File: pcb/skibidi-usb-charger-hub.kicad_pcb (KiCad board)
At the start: 4 copper layers, 85 x 90 mm, 92 parts, among them J1 USB_C_Receptacle_USB2.0_14P, J2 USB_C_Receptacle_USB2.0_14P, J3 USB_C_Receptacle_USB2.0_14P, J4 USB_C_Receptacle_USB2.0_14P, J5 USB_C_Receptacle_USB2.0_14P, J6 USB_C_Receptacle_USB2.0_14P, U10 IP6518, U11 USBLC6-4SC6, U12 IP6518, U13 USBLC6-4SC6, U14 IP6518, U15 USBLC6-4SC6, U16 IP6518, U17 USBLC6-4SC6, U3 NDP5102SE, U6 NDP5102SE, U9 NDP5102SE

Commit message: update art + gerbers + readme
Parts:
- added H23: 5V, extras:18AWG_Soldering_Hole, F.Cu at (125.0, 95.0)
- added H24: 5V, extras:18AWG_Soldering_Hole, F.Cu at (132.0, 95.0)
- added H25: 5V, extras:18AWG_Soldering_Hole, F.Cu at (139.0, 95.0)
- added H26: 12V, extras:18AWG_Soldering_Hole, F.Cu at (154.0, 95.0)
- added H27: 12V, extras:18AWG_Soldering_Hole, F.Cu at (161.0, 95.0)
- added H28: 12V, extras:18AWG_Soldering_Hole, F.Cu at (168.0, 95.0)
- added J10: Conn_02x01, Connector_PinHeader_2.54mm:PinHeader_2x01_P2.54mm_Vertical, F.Cu at (97.0, 64.0)
- added J7: Conn_02x01, Connector_PinHeader_2.54mm:PinHeader_2x01_P2.54mm_Vertical, F.Cu at (135.0, 138.0)
- added J8: Conn_02x01, Connector_PinHeader_2.54mm:PinHeader_2x01_P2.54mm_Vertical, F.Cu at (154.0, 138.0)
- added J9: Conn_02x01, Connector_PinHeader_2.54mm:PinHeader_2x01_P2.54mm_Vertical, F.Cu at (97.0, 84.0)
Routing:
- added copper zone on F.Cu, net GND
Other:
- board text added: "12V"
- board text added: "15A"
- board text added: "18AWG"
- board text added: "4xPD USB C: 9V 3A 2xUSB C: 5V 3A 4xUSB A: 5V 2.2A"
- board text added: "5V"
- board text added: "Designed in Canada"
- board text added: "GND"
- board text added: "M3"
- board text added: "Skibidi USB Charging Hub!"
- board text added: "Zip Tie"
- board text added: "toby@vsus.app"
- board text added: "tobycm.dev"

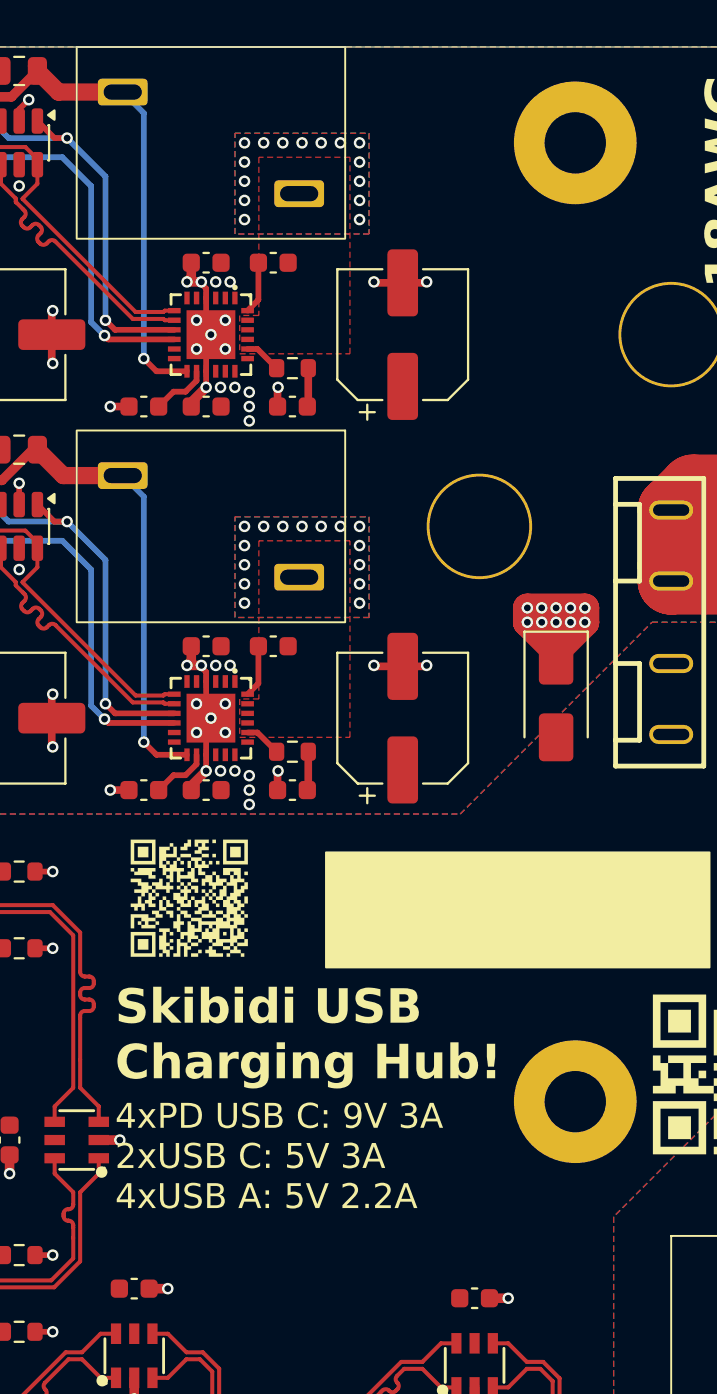
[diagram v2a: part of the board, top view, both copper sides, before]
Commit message: add pcbway gerber + back render + names on pcb back
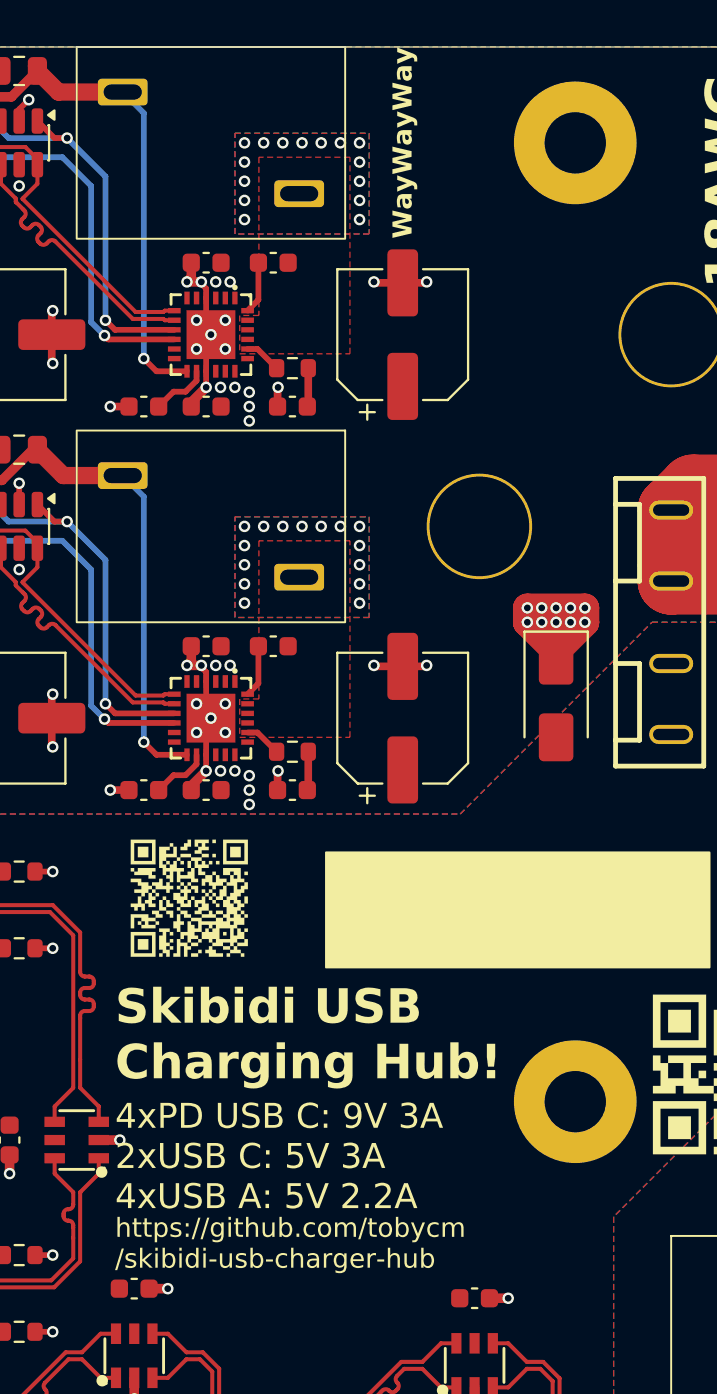
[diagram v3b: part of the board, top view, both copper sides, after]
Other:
- board text added: "@KaiPereira @ArcaEge @Rudy @deltea @Sir Jarquavius of Irkendale the Third"
- board text added: "@cubit010 @Tanuki @Drew @h @i10 @Tyson"
- board text added: "Honourable mentions: Pen High Hack Club (Kim, Kira, Nava, Ben, Jacob) Penticton Robotics Greyback Construction"
- board text added: "WayWayWay"
- board text added: "https://github.com/tobycm /skibidi-usb-charger-hub"
